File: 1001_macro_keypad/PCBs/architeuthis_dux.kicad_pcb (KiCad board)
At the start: 2 copper layers, 145.7 x 117.9 mm, 43 parts, among them J1 ePaperModule, J2 RotaryModule_01, J3 RotaryModule_02, SW01 MX_SW, SW10 MX_SW, SW11 MX_SW, SW12 MX_SW, SW13 MX_SW, SW14 MX_SW, SW2 MX_SW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

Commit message: pcb 완성, 3d모델 시작
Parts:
- moved REF** 22.8 mm to (149.0, 124.0)
- moved REF** 14.6 mm to (256.0, 97.0)
- moved REF** 12.4 mm to (185.0, 105.0)
- moved REF** 12.2 mm to (258.0, 158.0)
- moved REF** 12.2 mm to (169.0, 46.0)
- moved J3 11.6 mm to (253.7, 78.3)
- moved J2 11.6 mm to (253.7, 60.8)
- moved REF** 10.8 mm to (134.0, 59.0)
- moved SW13 1.05 mm to (245.0, 125.0), turned to -34.25 degrees
- moved REF** 1.00 mm to (258.0, 120.0)
- moved REF** 1.00 mm to (258.0, 39.0)
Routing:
- net +5V: track 70.0 -> 56.4 mm
- net COL2: track 252.2 -> 264.9 mm
- net ROW3: track 109.3 -> 119.5 mm
- net Net-(J2-S1): track 14.0 -> 24.3 mm
- net Net-(J2-S2): track 13.0 -> 21.7 mm
- net Net-(J2-KEY): track 13.0 -> 21.7 mm
- net COL3: track 196.5 -> 201.2 mm
- net Net-(J3-Pin_2): track 12.1 -> 14.5 mm
- net Net-(J3-Pin_3): track 32.0 -> 33.9 mm
- net Net-(J3-Pin_4): track 32.3 -> 33.9 mm
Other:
- board size 145.7 x 117.9 mm -> 147.5 x 126.1 mm

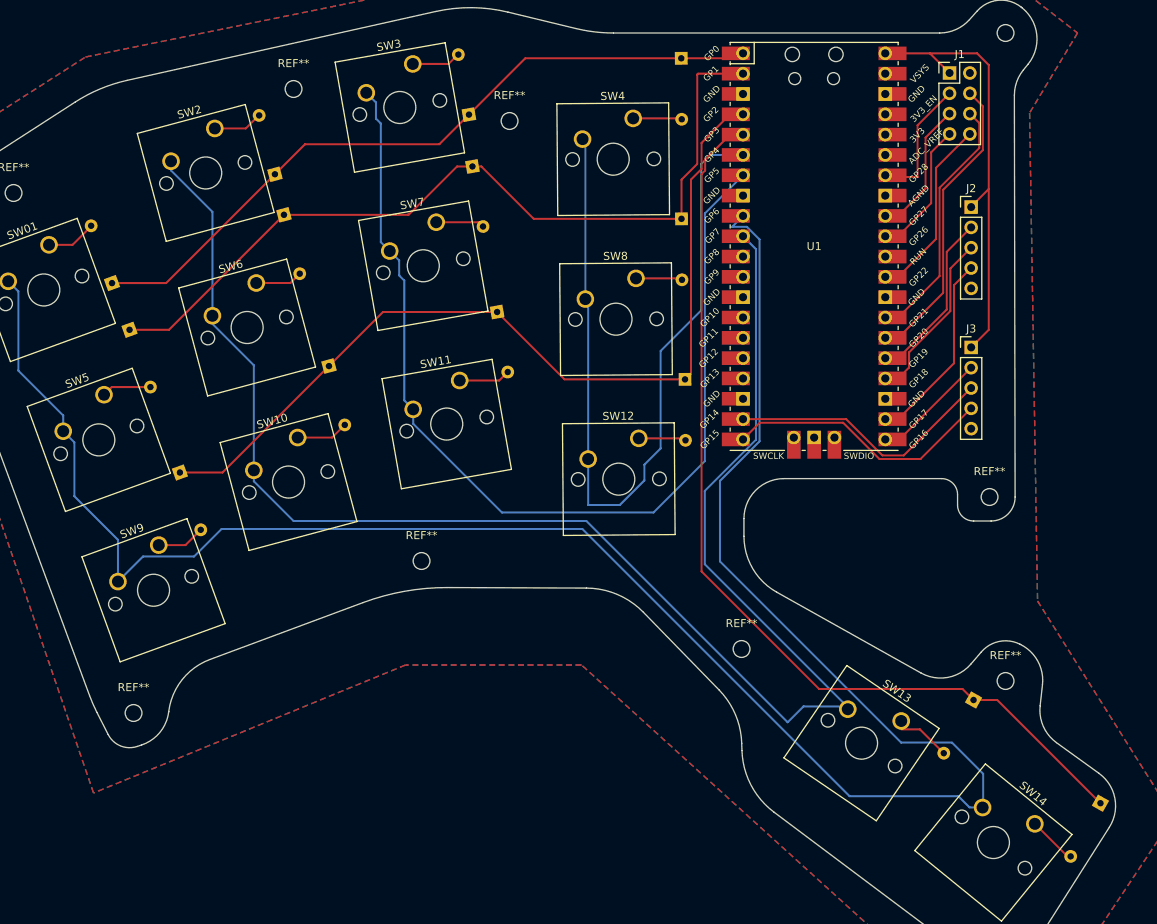
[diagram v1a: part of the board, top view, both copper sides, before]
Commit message: 펌웨어 추가, 다이오드 방향 변경 및 재배선
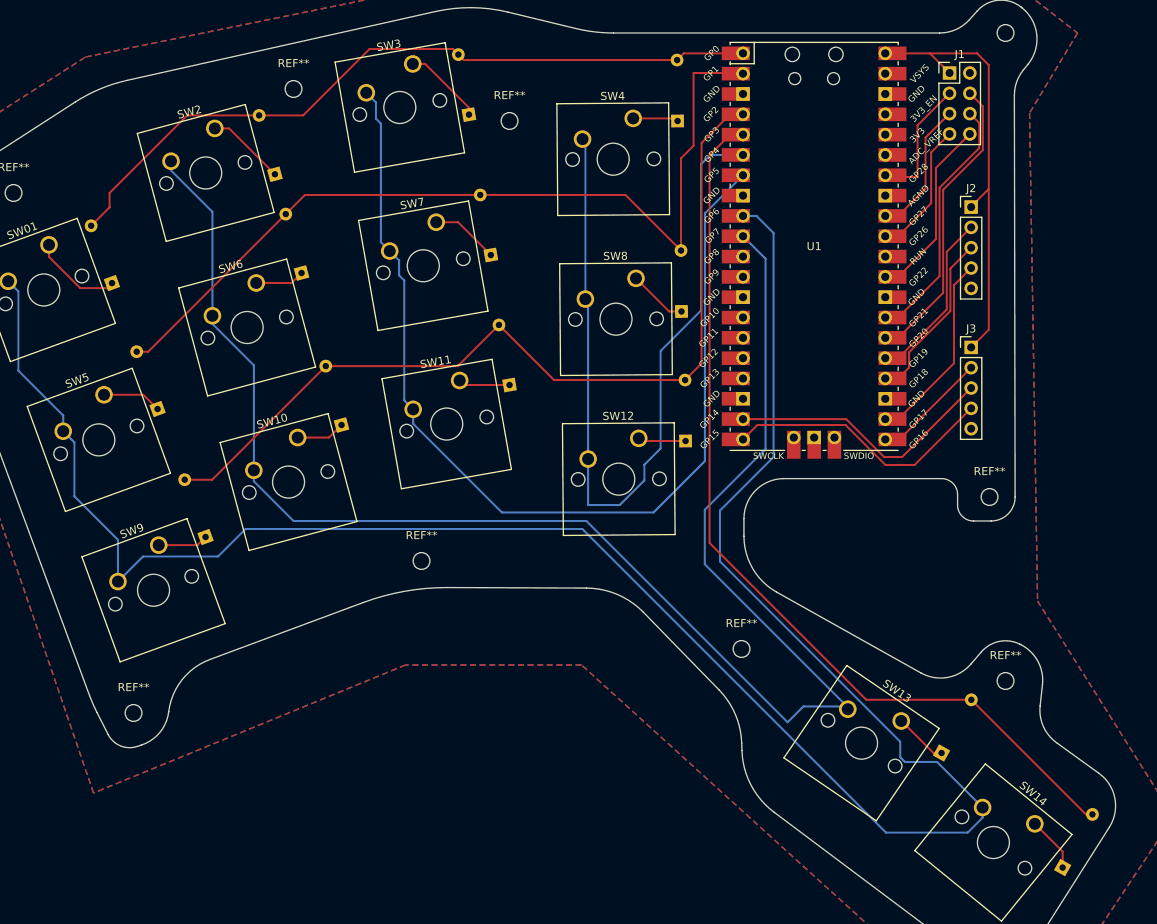
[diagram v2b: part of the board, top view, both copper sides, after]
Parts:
- moved D8 11.6 mm to (217.5, 73.8), turned to 90.45 degrees
- moved D7 11.3 mm to (193.7, 66.8), turned to 100 degrees
- moved D5 10.5 mm to (152.0, 86.0), turned to 110 degrees
- moved D14 9.33 mm to (265.1, 143.3), turned to 60.75 degrees
- moved D11 9.26 mm to (196.0, 83.0), turned to 100 degrees
- moved D9 8.67 mm to (158.0, 102.0), turned to 110 degrees
- moved D4 7.85 mm to (217.0, 50.0), turned to 90.45 degrees
- moved D13 7.74 mm to (250.0, 129.0), turned to 60.75 degrees
- moved D12 7.70 mm to (218.0, 90.0), turned to 90.45 degrees
- moved D6 7.60 mm to (170.0, 69.0), turned to 105 degrees
- moved D10 7.54 mm to (175.0, 88.0), turned to 105 degrees
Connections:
- D1 pad 1: ROW0 -> Net-(D1-K)
- D1 pad 2: Net-(D1-A) -> ROW0
- D10 pad 1: ROW2 -> Net-(D10-K)
- D10 pad 2: Net-(D10-A) -> ROW2
- D11 pad 1: ROW2 -> Net-(D11-K)
- D11 pad 2: Net-(D11-A) -> ROW2
- D12 pad 1: ROW2 -> Net-(D12-K)
- D12 pad 2: Net-(D12-A) -> ROW2
- D13 pad 1: ROW3 -> Net-(D13-K)
- D13 pad 2: Net-(D13-A) -> ROW3
- D14 pad 1: ROW3 -> Net-(D14-K)
- D14 pad 2: Net-(D14-A) -> ROW3
- D2 pad 1: ROW0 -> Net-(D2-K)
- D2 pad 2: Net-(D2-A) -> ROW0
- D3 pad 1: ROW0 -> Net-(D3-K)
- D3 pad 2: Net-(D3-A) -> ROW0
- D4 pad 1: ROW0 -> Net-(D4-K)
- D4 pad 2: Net-(D4-A) -> ROW0
- D5 pad 1: ROW1 -> Net-(D5-K)
- D5 pad 2: Net-(D5-A) -> ROW1
- D6 pad 1: ROW1 -> Net-(D6-K)
- D6 pad 2: Net-(D6-A) -> ROW1
- D7 pad 1: ROW1 -> Net-(D7-K)
- D7 pad 2: Net-(D7-A) -> ROW1
- D8 pad 1: ROW1 -> Net-(D8-K)
- D8 pad 2: Net-(D8-A) -> ROW1
- D9 pad 1: ROW2 -> Net-(D9-K)
- D9 pad 2: Net-(D9-A) -> ROW2
- SW01 pad 1: Net-(D1-A) -> Net-(D1-K)
- SW10 pad 1: Net-(D10-A) -> Net-(D10-K)
- SW11 pad 1: Net-(D11-A) -> Net-(D11-K)
- SW12 pad 1: Net-(D12-A) -> Net-(D12-K)
- SW13 pad 1: Net-(D13-A) -> Net-(D13-K)
- SW14 pad 1: Net-(D14-A) -> Net-(D14-K)
- SW2 pad 1: Net-(D2-A) -> Net-(D2-K)
- SW3 pad 1: Net-(D3-A) -> Net-(D3-K)
- SW4 pad 1: Net-(D4-A) -> Net-(D4-K)
- SW5 pad 1: Net-(D5-A) -> Net-(D5-K)
- SW6 pad 1: Net-(D6-A) -> Net-(D6-K)
- SW7 pad 1: Net-(D7-A) -> Net-(D7-K)
- SW8 pad 1: Net-(D8-A) -> Net-(D8-K)
- SW9 pad 1: Net-(D9-A) -> Net-(D9-K)
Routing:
- net Net-(D1-K): track 0.00 -> 11.3 mm
- net Net-(D3-K): track 0.00 -> 10.2 mm
- net Net-(D2-K): track 0.00 -> 9.89 mm
- net Net-(D7-K): track 0.00 -> 8.53 mm
- net Net-(D5-K): track 0.00 -> 7.43 mm
- net Net-(D8-K): track 0.00 -> 7.40 mm
- net Net-(D14-K): track 0.00 -> 6.90 mm
- net Net-(D13-K): track 0.00 -> 6.70 mm
- net Net-(D13-A): track 6.55 -> 0.00 mm
- net Net-(D10-A): track 6.54 -> 0.00 mm
- net Net-(D11-K): track 0.00 -> 6.47 mm
- net Net-(D1-A): track 6.46 -> 0.00 mm
- net Net-(D11-A): track 6.44 -> 0.00 mm
- net Net-(D9-K): track 0.00 -> 6.27 mm
- net Net-(D2-A): track 6.22 -> 0.00 mm
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
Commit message: epaper 테스트
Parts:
- removed the REF** at (327.1, 85.0)
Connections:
- J1 pad 1: +5V -> VSYS
- U1 pad 36: unconnected-(U1-3V3-Pad36) -> +5V
- U1 pad 39: unconnected-(U1-VSYS-Pad39) -> VSYS
- U1 pad 40: +5V -> unconnected-(U1-VBUS-Pad40)
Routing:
- net +5V: track 56.4 -> 70.8 mm
- net VSYS: track 0.00 -> 8.07 mm
- net COL2: track 267.0 -> 267.8 mm, vias 0 -> 1
- net COL3: vias 0 -> 1

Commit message: 설계 픽스 및 모델링 작업 시작
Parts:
- added REF**: MountingHole_2.1mm, MountingHole:MountingHole_2.1mm, F.Cu at (172.1, 62.9)
- added REF**: MountingHole_2.1mm, MountingHole:MountingHole_2.1mm, F.Cu at (193.0, 104.1)
- added REF**: MountingHole_2.1mm, MountingHole:MountingHole_2.1mm, F.Cu at (217.3, 106.9)
- added REF**: MountingHole_2.1mm, MountingHole:MountingHole_2.1mm, F.Cu at (197.0, 65.5)
- moved REF** 15.2 mm to (170.1, 107.9)
- moved D11 5.59 mm to (197.0, 88.5)
- moved REF** 5.54 mm to (229.5, 119.3)
- moved REF 3.20 mm to (258.5, 95.0)
- renumbered REF** to REF
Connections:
- U1 pad 11: unconnected-(U1-GPIO8-Pad11) -> Net-(J2-KEY)
- U1 pad 12: unconnected-(U1-GPIO9-Pad12) -> Net-(J2-S2)
- U1 pad 14: unconnected-(U1-GPIO10-Pad14) -> Net-(J2-S1)
- U1 pad 17: unconnected-(U1-GPIO13-Pad17) -> Net-(J3-Pin_2)
- U1 pad 21: Net-(J3-Pin_2) -> Net-(J1-SDA)
- U1 pad 22: Net-(J2-S1) -> Net-(J1-GND)
- U1 pad 24: Net-(J2-S2) -> Net-(J1-CS)
- U1 pad 25: Net-(J2-KEY) -> Net-(J1-D/C)
- U1 pad 26: Net-(J1-CS) -> Net-(J1-SCL)
- U1 pad 27: Net-(J1-SDA) -> Net-(J1-VCC)
- U1 pad 29: Net-(J1-VCC) -> unconnected-(U1-GPIO22-Pad29)
- U1 pad 31: Net-(J1-GND) -> unconnected-(U1-GPIO26_ADC0-Pad31)
- U1 pad 32: Net-(J1-SCL) -> unconnected-(U1-GPIO27_ADC1-Pad32)
- U1 pad 34: Net-(J1-D/C) -> unconnected-(U1-GPIO28_ADC2-Pad34)
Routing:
- net Net-(J1-D/C): track 16.2 -> 48.4 mm
- net Net-(J1-CS): track 37.2 -> 62.2 mm
- net Net-(J1-GND): track 17.1 -> 39.9 mm
- net Net-(J1-SCL): track 17.1 -> 35.8 mm
- net Net-(J1-SDA): track 31.8 -> 47.0 mm
- net Net-(J3-Pin_2): track 14.5 -> 29.1 mm
- net Net-(J1-VCC): track 23.2 -> 31.7 mm
- net Net-(J2-KEY): track 21.7 -> 30.2 mm
- net Net-(J2-S2): track 21.7 -> 30.0 mm
- net Net-(J2-S1): track 24.3 -> 31.1 mm
- net ROW2: track 110.6 -> 106.3 mm
- net Net-(D11-K): track 6.47 -> 9.54 mm
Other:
- outline, holes or cut-outs redrawn
